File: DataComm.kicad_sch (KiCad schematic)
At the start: 3 parts, among them J1 ESQ-126-39-G-D, J2 ESQ-126-39-G-D, U1 STM32U595RJTx

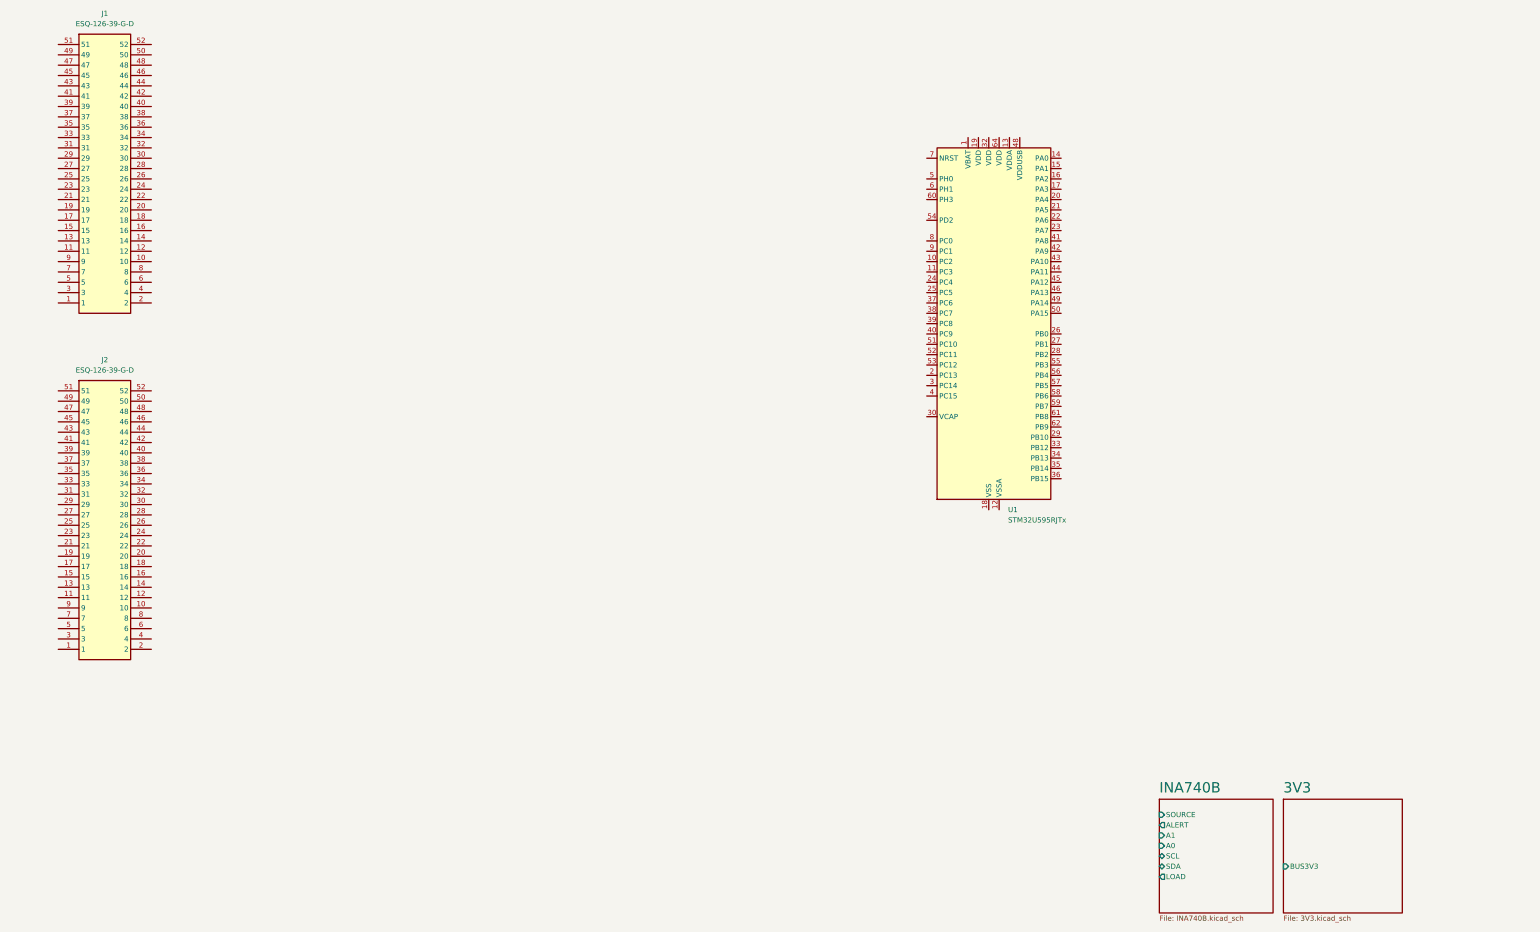
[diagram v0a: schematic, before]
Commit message: Buck-boost 5V entry
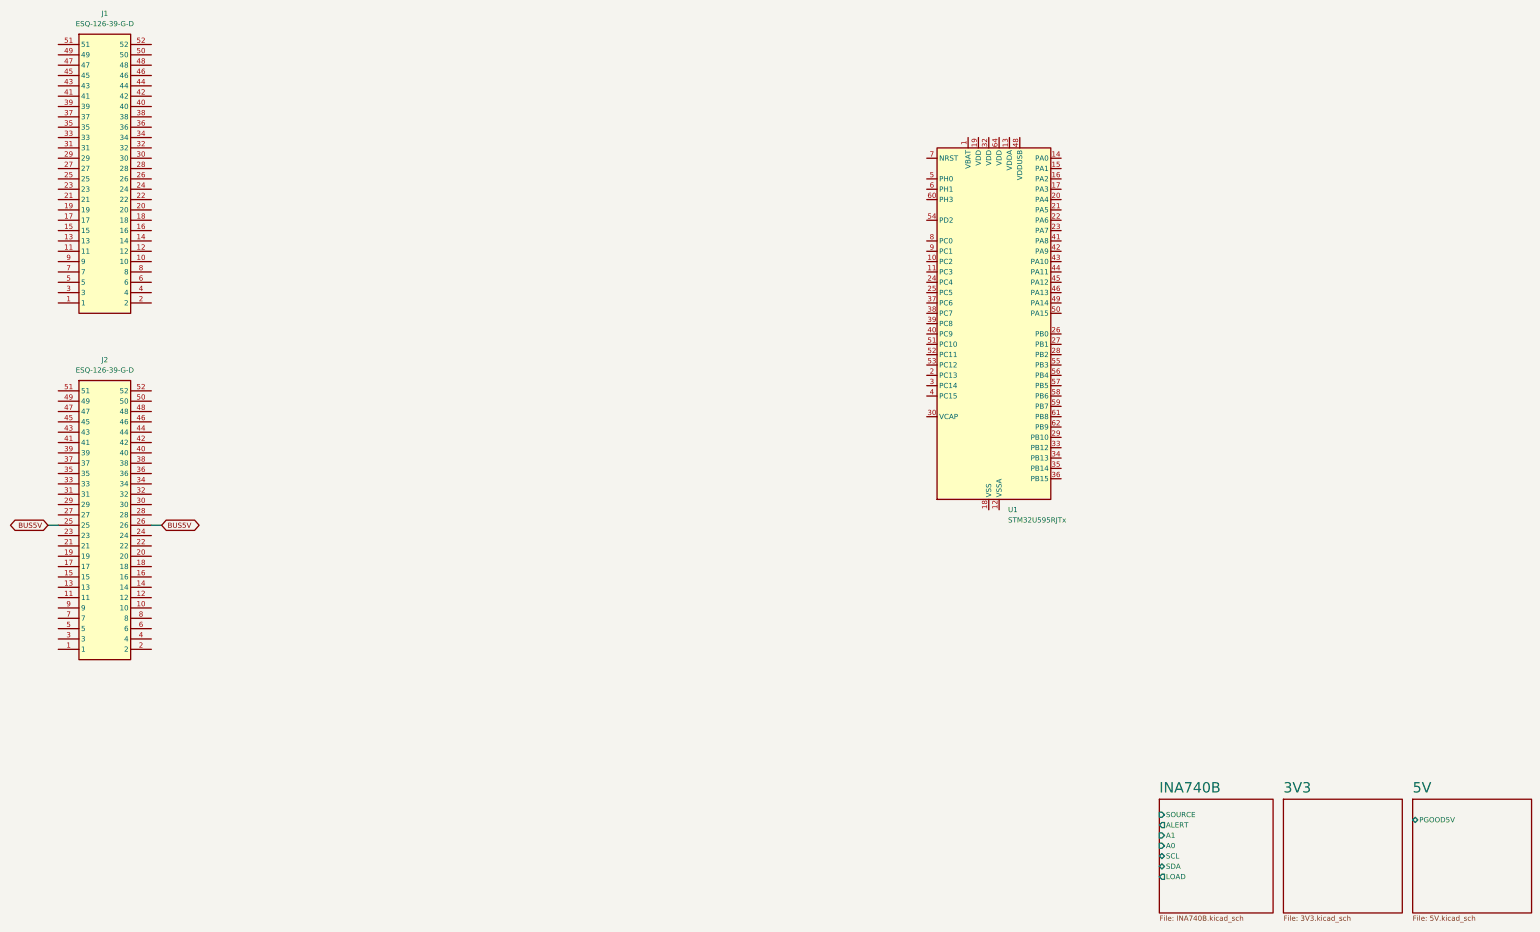
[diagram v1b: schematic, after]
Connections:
- net BUS5V: now reaches J2.25
- net BUS5V: now also J2.26
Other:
- added sheet 5V (5V.kicad_sch)
- sheet 3V3 ports: added none; removed BUS3V3
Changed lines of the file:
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@@
 	(generator_version "8.0")
 	(paper "USLedger")
+	(wire
+		(pts
+			(xy 57.15 177.8) (xy 59.69 177.8)
+		)
+		(stroke
+			(width 0)
+			(type default)
+		)
+	)
+	(wire
+		(pts
+			(xy 82.55 177.8) (xy 85.09 177.8)
+		)
+		(stroke
+			(width 0)
+			(type default)
+		)
+	)
+	(global_label "BUS5V"
+		(shape bidirectional)
+		(at 57.15 177.8 180)
+		(fields_autoplaced yes)
+		(effects
+			(font
+				(size 1.27 1.27)
+			)
+			(justify right)
+		)
+		(property "Intersheetrefs" "${INTERSHEET_REFS}"
+			(at 46.9454 177.8 0)
+			(effects
+				(font
+					(size 1.27 1.27)
+				)
+				(justify right)
+				(hide yes)
+			)
+		)
+	)
+	(global_label "BUS5V"
+		(shape bidirectional)
+		(at 85.09 177.8 0)
+		(fields_autoplaced yes)
+		(effects
+			(font
+				(size 1.27 1.27)
+			)
+			(justify left)
+		)
+		(property "Intersheetrefs" "${INTERSHEET_REFS}"
+			(at 95.2946 177.8 0)
+			(effects
+				(font
+					(size 1.27 1.27)
+				)
+				(justify left)
+				(hide yes)
+			)
+		)
+	)
 	(symbol
 		(lib_id "MCU_ST_STM32U5:STM32U595RJTx")
@@
 	)
 	(sheet
+		(at 392.43 245.11)
+		(size 29.21 27.94)
+		(fields_autoplaced yes)
+		(stroke
+			(width 0.1524)
+			(type solid)
+		)
+		(fill
+			(color 0 0 0 0.0000)
+		)
+		(property "Sheetname" "5V"
+			(at 392.43 243.7634 0)
+			(effects
+				(font
+					(size 2.54 2.54)
+				)
+				(justify left bottom)
+			)
+		)
+		(property "Sheetfile" "5V.kicad_sch"
+			(at 392.43 273.6346 0)
+			(effects
+				(font
+					(size 1.27 1.27)
+				)
+				(justify left top)
+			)
+		)
+		(pin "PGOOD5V" bidirectional
+			(at 392.43 250.19 180)
+			(effects
+				(font
+					(size 1.27 1.27)
+				)
+				(justify left)
+			)
+		)
+		(instances
+			(project "DataComm"
+				(path "/c2737be1-67a7-478e-8d11-58cc77864a99"
+					(page "3")
+				)
+			)
+		)
+	)
+	(sheet
 		(at 360.68 245.11)
 		(size 29.21 27.94)
@@
 			)
 		)
-		(pin "BUS3V3" input
-			(at 360.68 261.62 180)
-			(effects
-				(font
-					(size 1.27 1.27)
-				)
-				(justify left)
-			)
-		)
